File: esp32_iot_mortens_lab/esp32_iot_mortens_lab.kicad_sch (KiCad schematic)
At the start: 38 parts, among them J1 Conn_01x04, J2 Screw_Terminal_01x03, J3 Screw_Terminal_01x08, J4 Screw_Terminal_01x02, J5 USB_C_Receptacle_USB2.0_16P, K1 RT314A05, Q1 UMH3N, Q2 BC817, SW1 SW_Push, U1 ESP32-WROOM-32D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

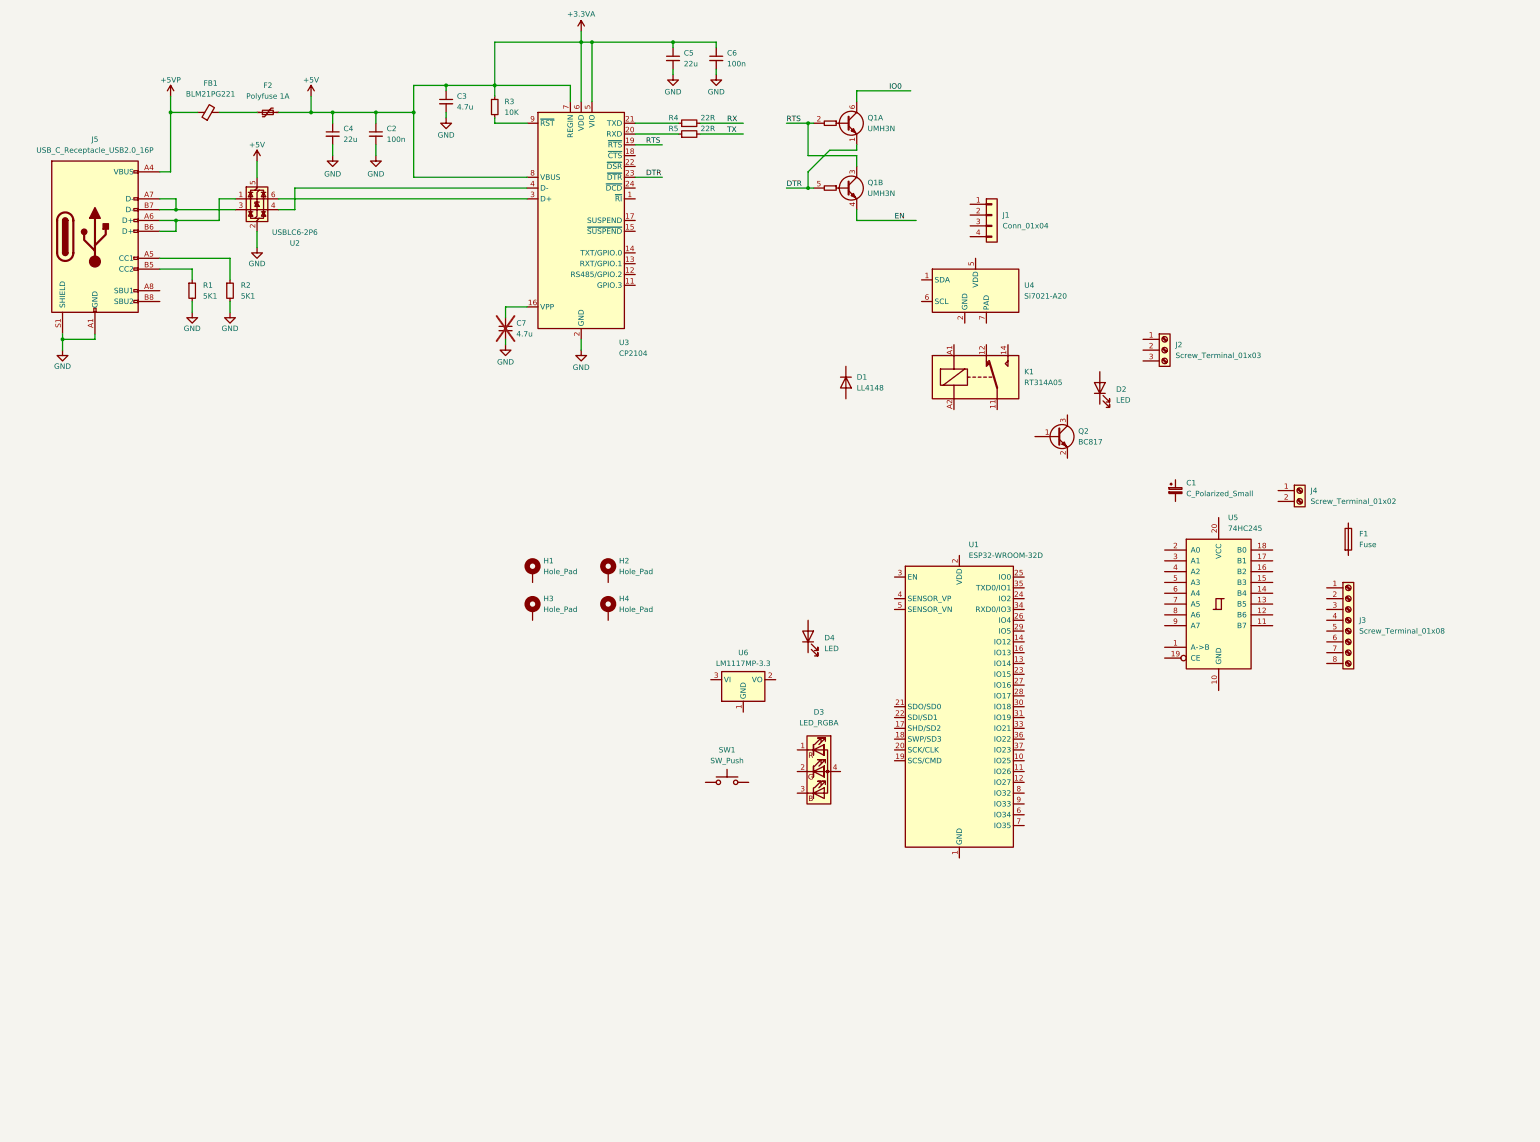
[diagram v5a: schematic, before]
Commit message: upto LDO and LED subcircuits
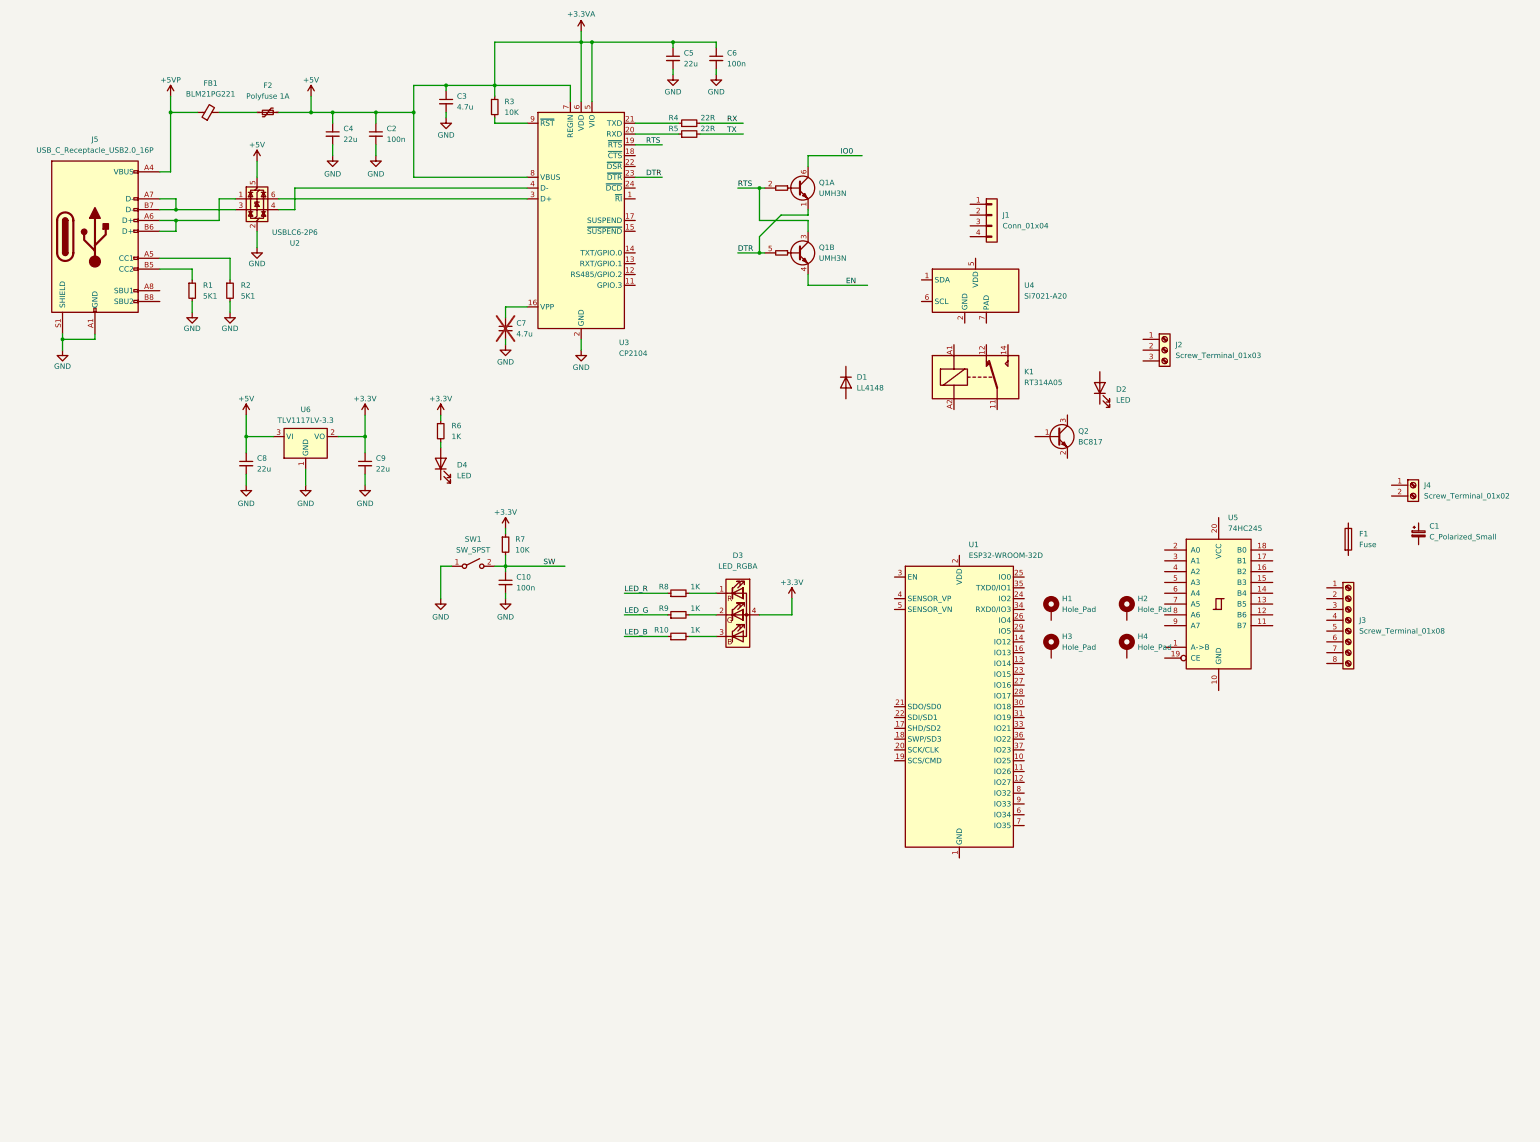
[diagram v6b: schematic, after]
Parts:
- removed SW1: SW_Push, symbol Switch:SW_Push
- added C10: 100n, symbol Device:C_Small
- added C8, C9: 22u, symbol Device:C_Small
- added R10, R6, R8, R9: 1K, symbol Device:R_Small
- added R7: 10K, symbol Device:R_Small
- added SW1: SW_SPST, symbol Switch:SW_SPST
- U6: value LM1117MP-3.3 -> TLV1117LV-3.3
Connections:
- net +3.3VA: now also U6.3 (VI), C8.1
- net GND: now also U6.1 (GND), C10.2, C8.2, C9.2, SW1.1 (A)
- net at D4.2 (A): now also R6.2
- net at D3.1 (RK): now also R8.2
- net at D3.2 (GK): now also R9.2
- net at D3.3 (BK): now also R10.2
- net +3.3V: now reaches D3.4 (A)
- net +3.3V: now also U6.2 (VO), C9.1, R6.1, R7.1
- new net LED_B: R10.1
- new net LED_G: R9.1
- new net LED_R: R8.1
- new net SW: C10.1, R7.2, SW1.2 (B)
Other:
- moved on the sheet: C1, D3, D4, H1, H2, H3, H4, J4, Q1A, Q1B, U6

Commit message: qwiic connector
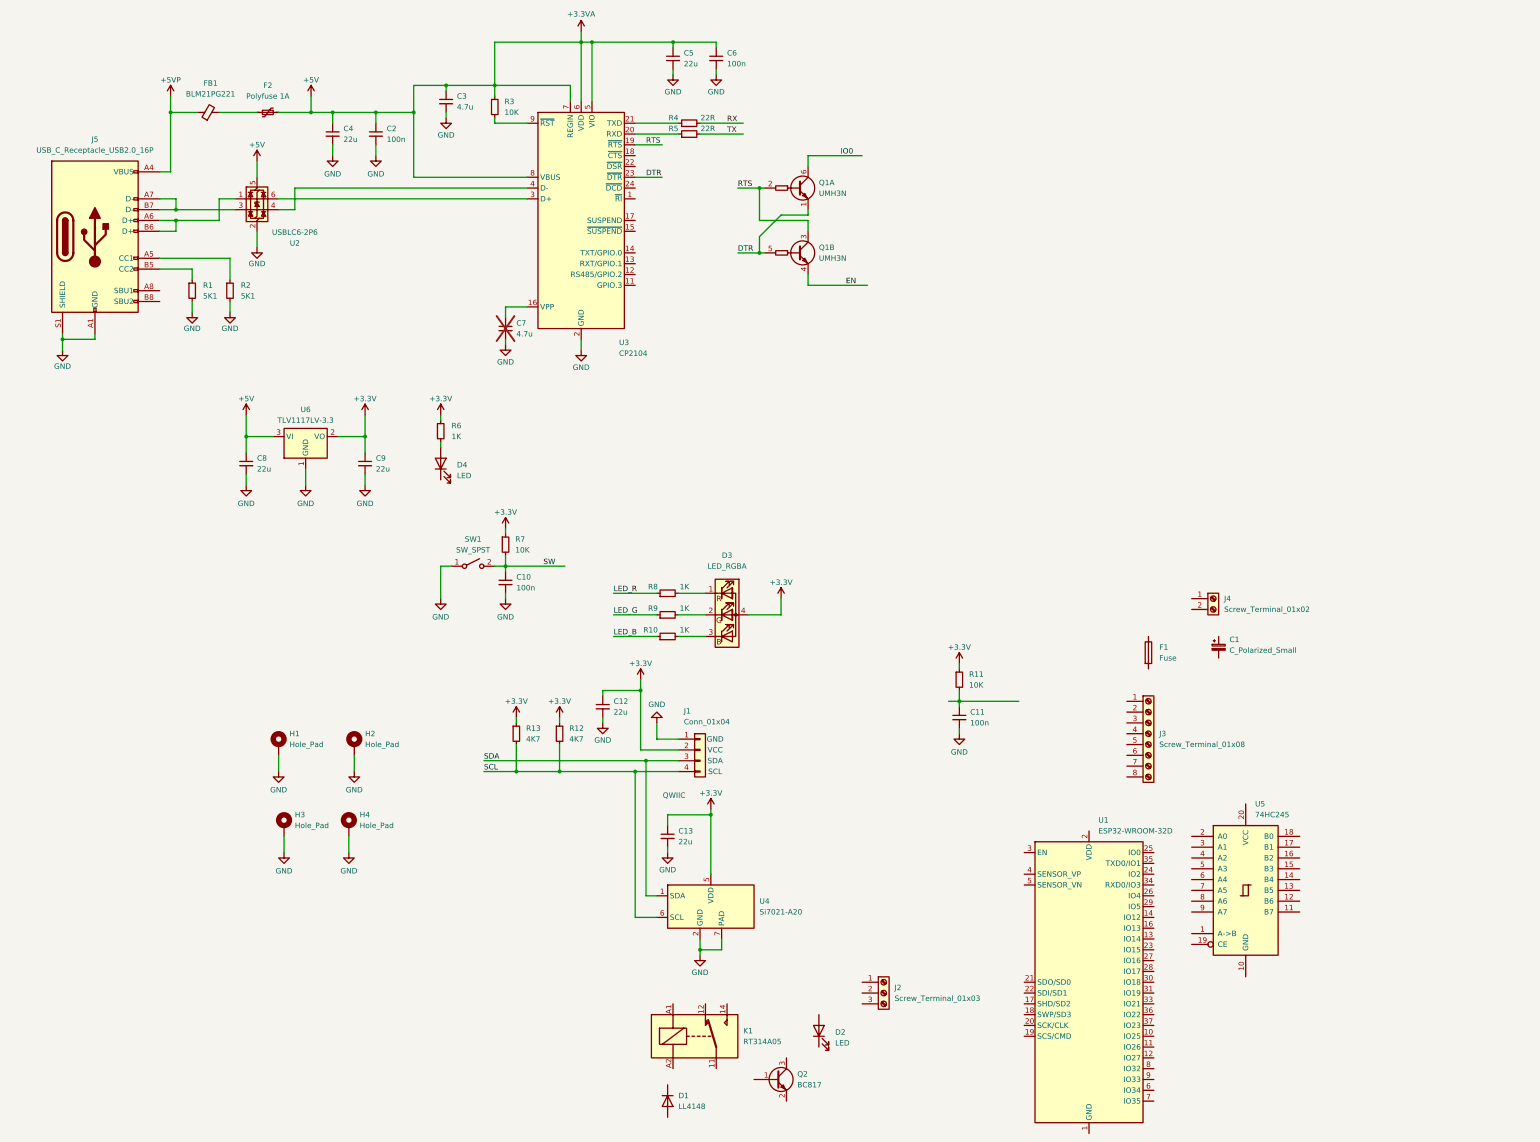
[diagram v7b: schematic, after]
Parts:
- added C11: 100n, symbol Device:C_Small
- added C12, C13: 22u, symbol Device:C_Small
- added R11: 10K, symbol Device:R_Small
- added R12, R13: 4K7, symbol Device:R_Small
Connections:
- net +3.3V: now also J1.2 (Pin_2), U4.5 (VDD), C12.1, C13.1, R11.1, R12.1, R13.1
- net GND: now also H1.1, H2.1, H3.1, H4.1, J1.1 (Pin_1), U4.2 (GND), U4.7 (PAD), C11.2, C12.2, C13.2
- net SDA: now reaches U4.1 (SDA)
- net SDA: now also J1.3 (Pin_3)
- net SCL: now reaches U4.6 (SCL)
- net SCL: now also J1.4 (Pin_4), R12.2, R13.2
- new net: C11.1, R11.2
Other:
- note added: "GND"
- note added: "QWIIC"
- note added: "SCL"
- note added: "SDA"
- note added: "VCC"
- moved on the sheet: C1, D1, D2, D3, F1, H1, H2, H3, H4, J1, J2, J3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

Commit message: relay subcircuit
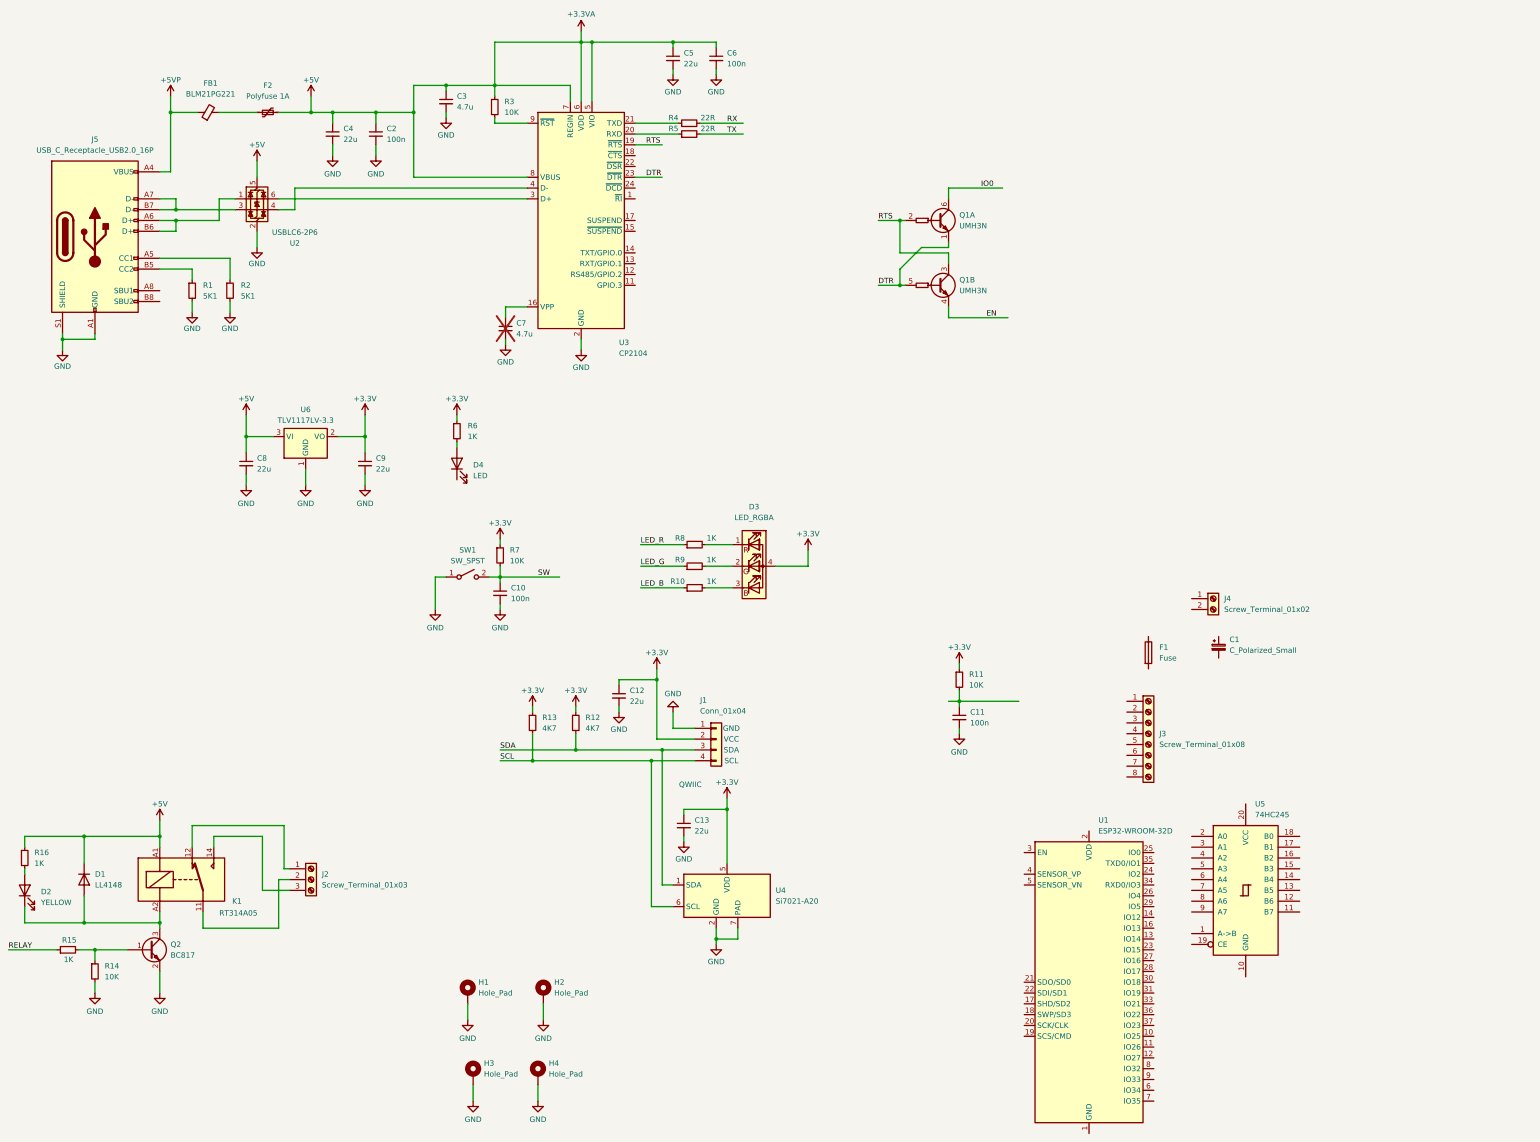
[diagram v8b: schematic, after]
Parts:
- added R14: 10K, symbol Device:R_Small
- added R15, R16: 1K, symbol Device:R_Small
- D2: value LED -> YELLOW
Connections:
- net +3.3VA: now also D1.1 (K), K1.A1, R16.1
- net GND: now also Q2.2 (E), R14.2
- net SCL: no longer R12.2
- net SDA: now also R12.2
- net at D2.1 (K): now also D1.2 (A), K1.A2, Q2.3 (C)
- net at D2.2 (A): now also R16.2
- net at Q2.1 (B): now also R14.1, R15.2
- net at J2.1 (Pin_1): now also K1.12
- net at J2.2 (Pin_2): now also K1.11
- net at J2.3 (Pin_3): now also K1.14
- new net RELAY: R15.1
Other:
- moved on the sheet: C10, C12, C13, D1, D2, D3, D4, H1, H2, H3, H4, J1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
